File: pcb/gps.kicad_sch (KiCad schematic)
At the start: 16 parts, among them J14 PPS, J15 U.FL, U12 MAX-M10S-00B, U13 TPS22941

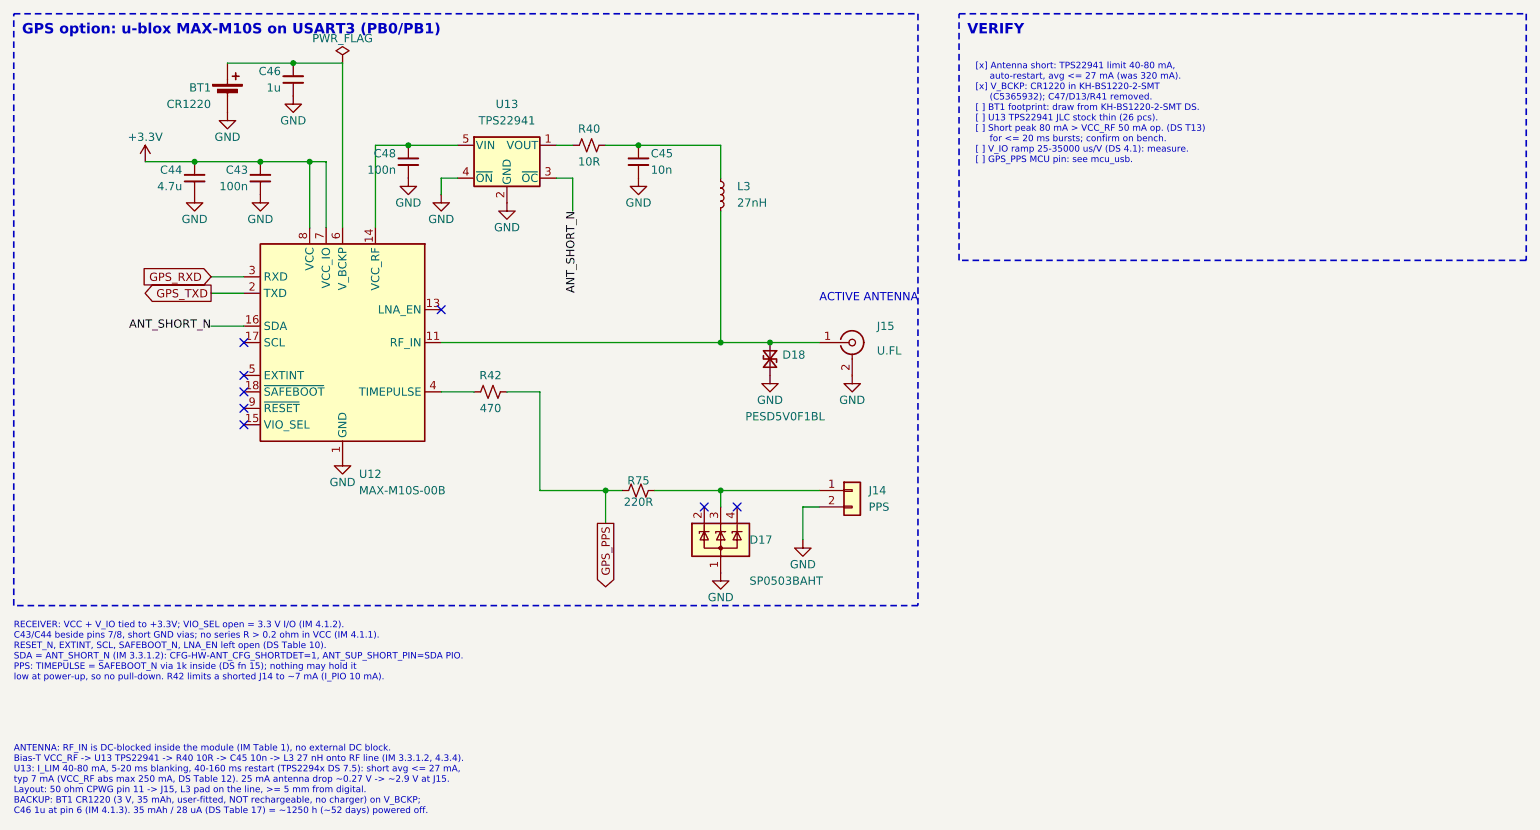
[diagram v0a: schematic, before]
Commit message: Rev C layout: board grown to 130x110 mm, headers J4/J5/J8/J10/J14 removed, power rework layout
- Outline grown 10 mm on top and left edges (130x110 mm); locked edge parts moved with outline
- Removed J4, J5, J8, J10, J14 and support parts (D13-D15, D17, D19, D20, R64-R67, R69-R71, R75-R79); UPDI J13 kept
- Power rework placed and routed (TPS61085 boost, INA193 U14, Q10 soft-start)
- Y1 placed at U9, stray passives moved, silkscreen labels cleaned up
- Routed: DRC 0 errors / 0 unconnected, schematic parity 0, ERC 0; layout gate 11/11
- DRU: ESC_* fine-pitch escape 0.20 mm rule areas, U1 pad-to-pad 0.14 mm
- In2 keep-away waivers (GND-plane shielded): Q2 drain, MCU_TX, MCU_RX near R6, 22.6 mm MCU_RX run near U9
- Libs: 6x6 H13 switch, OLED pin-header module footprint, updated symbols
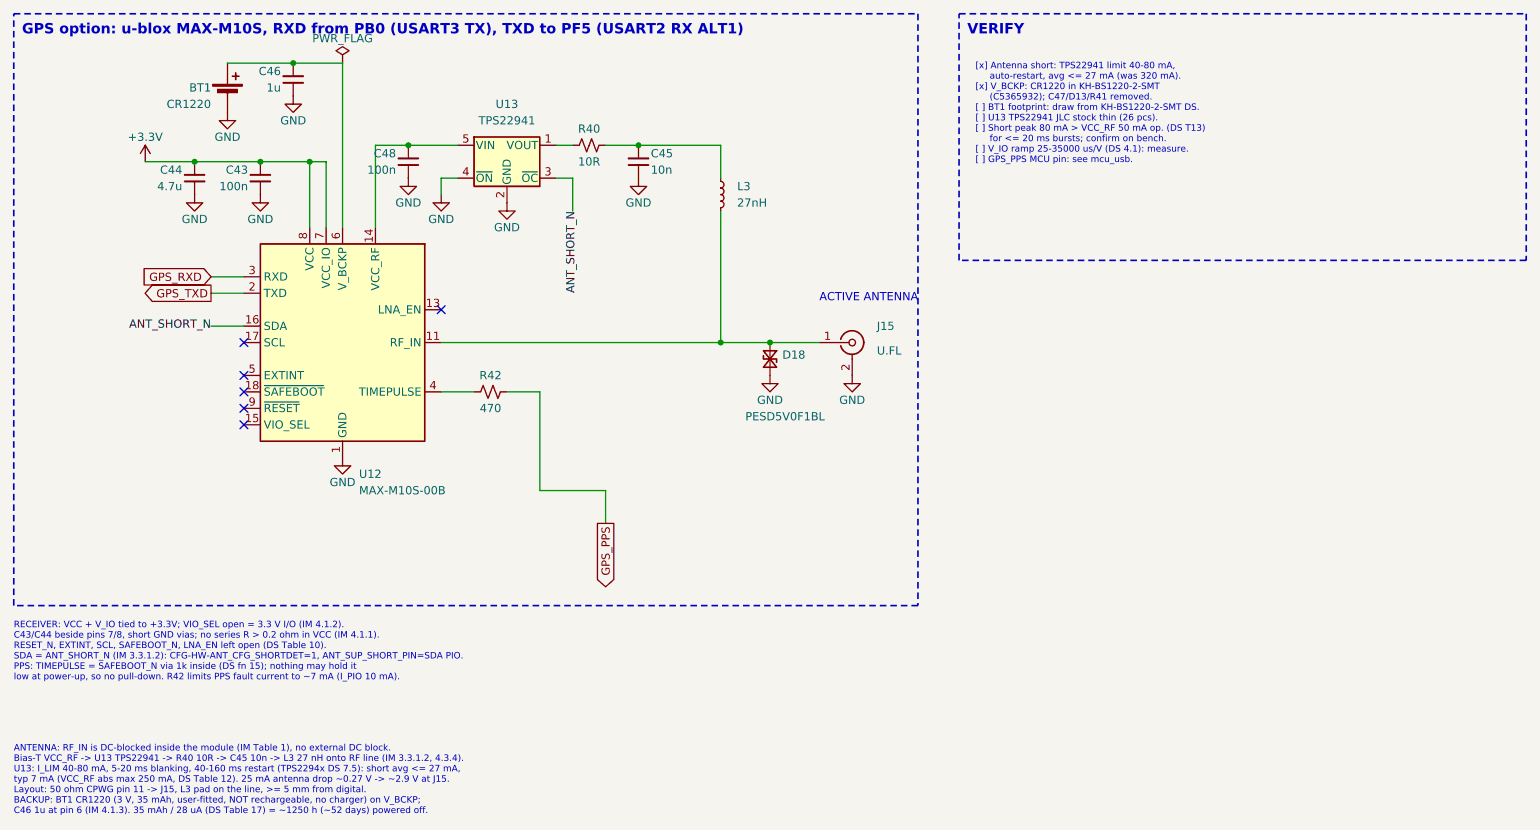
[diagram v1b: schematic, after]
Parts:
- removed D17: SP0503BAHT, Package_TO_SOT_SMD:SOT-143, symbol Power_Protection:SP0503BAHT
- removed J14: PPS, Connector_PinHeader_2.54mm:PinHeader_1x02_P2.54mm_Vertical, symbol Connector_Generic:Conn_01x02
- removed R75: 220R, Resistor_SMD:R_0805_2012Metric, symbol Device:R_Small_US
- C46: footprint Capacitor_SMD:C_0805_2012Metric -> Capacitor_SMD:C_0402_1005Metric; LCSC C28323 -> C52923; MPN CL21B105KBFNNNE -> CL05A105KA5NQNC
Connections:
- no-connect marks 8 -> 6
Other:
- note added: "GPS option: u-blox MAX-M10S, RXD from PB0 (USART3 TX), TXD to PF5 (USART2 RX ALT1)"
- note removed: "GPS option: u-blox MAX-M10S on USART3 (PB0/PB1)"

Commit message: Renumber all references monotonically 1..N per prefix; sync PCB silk labels and auto-named nets; ERC 0, DRC 0/0
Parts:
- renumbered C46 to C103, C48 to C104, C45 to C105, C44 to C106, C43 to C107, D18 to D13, J15 to J8, L3 to L15, R40 to R41, U13 to U10, U12 to U11
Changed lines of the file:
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@@
 		(on_board yes)
 		(dnp no)
-		(property "Reference" "U12"
+		(property "Reference" "U11"
 			(at 104.14 144.78 0)
 			(effects
@@
 			(project "OpenBeacon2"
 				(path "/046319a3-a6ce-4e59-a888-94e340127381/a3f6c2d4-5b7e-4f10-9c8d-2e4b6a8c0d12"
-					(reference "U12")
+					(reference "U11")
 					(unit 1)
 				)
@@
 		(on_board yes)
 		(dnp no)
-		(property "Reference" "C43"
+		(property "Reference" "C107"
 			(at 86.995 97.79 0)
 			(effects
@@
 			(project "OpenBeacon2"
 				(path "/046319a3-a6ce-4e59-a888-94e340127381/a3f6c2d4-5b7e-4f10-9c8d-2e4b6a8c0d12"
-					(reference "C43")
+					(reference "C107")
 					(unit 1)
 				)
@@
 		(on_board yes)
 		(dnp no)
-		(property "Reference" "#PWR1001"
+		(property "Reference" "#PWR116"
 			(at 88.9 101.6 0)
 			(effects
@@
 			(project "OpenBeacon2"
 				(path "/046319a3-a6ce-4e59-a888-94e340127381/a3f6c2d4-5b7e-4f10-9c8d-2e4b6a8c0d12"
-					(reference "#PWR1001")
+					(reference "#PWR116")
 					(unit 1)
 				)
@@
 		(on_board yes)
 		(dnp no)
-		(property "Reference" "C44"
+		(property "Reference" "C106"
 			(at 76.835 97.79 0)
 			(effects
@@
 			(project "OpenBeacon2"
 				(path "/046319a3-a6ce-4e59-a888-94e340127381/a3f6c2d4-5b7e-4f10-9c8d-2e4b6a8c0d12"
-					(reference "C44")
+					(reference "C106")
 					(unit 1)
 				)
@@
 		(on_board yes)
 		(dnp no)
-		(property "Reference" "#PWR1002"
+		(property "Reference" "#PWR115"
 			(at 78.74 101.6 0)
 			(effects
@@
 			(project "OpenBeacon2"
 				(path "/046319a3-a6ce-4e59-a888-94e340127381/a3f6c2d4-5b7e-4f10-9c8d-2e4b6a8c0d12"
-					(reference "#PWR1002")
+					(reference "#PWR115")
 					(unit 1)
 				)
@@
 		(on_board yes)
 		(dnp no)
-		(property "Reference" "#PWR1003"
+		(property "Reference" "#PWR112"
 			(at 71.12 96.52 0)
 			(effects
@@
 			(project "OpenBeacon2"
 				(path "/046319a3-a6ce-4e59-a888-94e340127381/a3f6c2d4-5b7e-4f10-9c8d-2e4b6a8c0d12"
-					(reference "#PWR1003")
+					(reference "#PWR112")
 					(unit 1)
 				)
@@
 		(on_board yes)
 		(dnp no)
-		(property "Reference" "#PWR1004"
+		(property "Reference" "#PWR121"
 			(at 101.6 142.24 0)
 			(effects
@@
 			(project "OpenBeacon2"
 				(path "/046319a3-a6ce-4e59-a888-94e340127381/a3f6c2d4-5b7e-4f10-9c8d-2e4b6a8c0d12"
-					(reference "#PWR1004")
+					(reference "#PWR121")
 					(unit 1)
 				)
@@
 		(on_board yes)
 		(dnp no)
-		(property "Reference" "#FLG905"
+		(property "Reference" "#FLG5"
 			(at 101.6 81.28 0)
 			(effects
@@
 			(project "OpenBeacon2"
 				(path "/046319a3-a6ce-4e59-a888-94e340127381/a3f6c2d4-5b7e-4f10-9c8d-2e4b6a8c0d12"
-					(reference "#FLG905")
+					(reference "#FLG5")
 					(unit 1)
 				)
@@
 		(on_board yes)
 		(dnp no)
-		(property "Reference" "C46"
+		(property "Reference" "C103"
 			(at 92.075 82.55 0)
 			(effects
@@
 			(project "OpenBeacon2"
 				(path "/046319a3-a6ce-4e59-a888-94e340127381/a3f6c2d4-5b7e-4f10-9c8d-2e4b6a8c0d12"
-					(reference "C46")
+					(reference "C103")
 					(unit 1)
 				)
@@
 		(on_board yes)
 		(dnp no)
-		(property "Reference" "#PWR1005"
+		(property "Reference" "#PWR110"
 			(at 93.98 86.36 0)
 			(effects
@@
 			(project "OpenBeacon2"
 				(path "/046319a3-a6ce-4e59-a888-94e340127381/a3f6c2d4-5b7e-4f10-9c8d-2e4b6a8c0d12"
-					(reference "#PWR1005")
+					(reference "#PWR110")
 					(unit 1)
 				)
@@
 		(on_board yes)
 		(dnp no)
-		(property "Reference" "#PWR1006"
+		(property "Reference" "#PWR111"
 			(at 83.82 88.9 0)
 			(effects
@@
 			(project "OpenBeacon2"
 				(path "/046319a3-a6ce-4e59-a888-94e340127381/a3f6c2d4-5b7e-4f10-9c8d-2e4b6a8c0d12"
-					(reference "#PWR1006")
+					(reference "#PWR111")
 					(unit 1)
 				)
@@
 		(on_board yes)
 		(dnp no)
-		(property "Reference" "U13"
+		(property "Reference" "U10"
 			(at 127 87.63 0)
 			(effects
@@
 			(project "OpenBeacon2"
 				(path "/046319a3-a6ce-4e59-a888-94e340127381/a3f6c2d4-5b7e-4f10-9c8d-2e4b6a8c0d12"
-					(reference "U13")
+					(reference "U10")
 					(unit 1)
 				)
@@
 		(on_board yes)
 		(dnp no)
-		(property "Reference" "C48"
+		(property "Reference" "C104"
 			(at 109.855 95.25 0)
 			(effects
@@
 			(project "OpenBeacon2"
 				(path "/046319a3-a6ce-4e59-a888-94e340127381/a3f6c2d4-5b7e-4f10-9c8d-2e4b6a8c0d12"
-					(reference "C48")
+					(reference "C104")
 					(unit 1)
 				)
@@
 		(on_board yes)
 		(dnp no)
-		(property "Reference" "#PWR1007"
+		(property "Reference" "#PWR113"
 			(at 111.76 99.06 0)
 			(effects
@@
 			(project "OpenBeacon2"
 				(path "/046319a3-a6ce-4e59-a888-94e340127381/a3f6c2d4-5b7e-4f10-9c8d-2e4b6a8c0d12"
-					(reference "#PWR1007")
+					(reference "#PWR113")
 					(unit 1)
 				)
@@
 		(on_board yes)
 		(dnp no)
-		(property "Reference" "#PWR1008"
+		(property "Reference" "#PWR117"
 			(at 116.84 101.6 0)
 			(effects
@@
 			(project "OpenBeacon2"
 				(path "/046319a3-a6ce-4e59-a888-94e340127381/a3f6c2d4-5b7e-4f10-9c8d-2e4b6a8c0d12"
-					(reference "#PWR1008")
+					(reference "#PWR117")
 					(unit 1)
 				)
@@
 		(on_board yes)
 		(dnp no)
-		(property "Reference" "#PWR1009"
+		(property "Reference" "#PWR118"
 			(at 127 102.87 0)
 			(effects
@@
 			(project "OpenBeacon2"
 				(path "/046319a3-a6ce-4e59-a888-94e340127381/a3f6c2d4-5b7e-4f10-9c8d-2e4b6a8c0d12"
-					(reference "#PWR1009")
+					(reference "#PWR118")
 					(unit 1)
 				)
@@
 		(on_board yes)
 		(dnp no)
-		(property "Reference" "R40"
+		(property "Reference" "R41"
 			(at 139.7 91.44 90)
 			(effects
@@
 			(project "OpenBeacon2"
 				(path "/046319a3-a6ce-4e59-a888-94e340127381/a3f6c2d4-5b7e-4f10-9c8d-2e4b6a8c0d12"
-					(reference "R40")
+					(reference "R41")
 					(unit 1)
 				)
@@
 		(on_board yes)
 		(dnp no)
-		(property "Reference" "C45"
+		(property "Reference" "C105"
 			(at 149.225 95.25 0)
 			(effects
@@
 			(project "OpenBeacon2"
 				(path "/046319a3-a6ce-4e59-a888-94e340127381/a3f6c2d4-5b7e-4f10-9c8d-2e4b6a8c0d12"
-					(reference "C45")
+					(reference "C105")
 					(unit 1)
 				)
@@
 		(on_board yes)
 		(dnp no)
-		(property "Reference" "#PWR1010"
+		(property "Reference" "#PWR114"
 			(at 147.32 99.06 0)
 			(effects
@@
 			(project "OpenBeacon2"
 				(path "/046319a3-a6ce-4e59-a888-94e340127381/a3f6c2d4-5b7e-4f10-9c8d-2e4b6a8c0d12"
-					(reference "#PWR1010")
+					(reference "#PWR114")
 					(unit 1)
 				)
@@
 		(on_board yes)
 		(dnp no)
-		(property "Reference" "L3"
+		(property "Reference" "L15"
 			(at 162.56 100.33 0)
 			(effects
@@
 			(project "OpenBeacon2"
 				(path "/046319a3-a6ce-4e59-a888-94e340127381/a3f6c2d4-5b7e-4f10-9c8d-2e4b6a8c0d12"
-					(reference "L3")
+					(reference "L15")
 					(unit 1)
 				)
@@
 		(on_board yes)
 		(dnp no)
-		(property "Reference" "J15"
+		(property "Reference" "J8"
 			(at 184.15 121.92 0)
 			(effects
@@
 			(project "OpenBeacon2"
 				(path "/046319a3-a6ce-4e59-a888-94e340127381/a3f6c2d4-5b7e-4f10-9c8d-2e4b6a8c0d12"
-					(reference "J15")
+					(reference "J8")
 					(unit 1)
 				)
@@
 		(on_board yes)
 		(dnp no)
-		(property "Reference" "#PWR1011"
+		(property "Reference" "#PWR120"
 			(at 180.34 129.54 0)
 			(effects
@@
 			(project "OpenBeacon2"
 				(path "/046319a3-a6ce-4e59-a888-94e340127381/a3f6c2d4-5b7e-4f10-9c8d-2e4b6a8c0d12"
-					(reference "#PWR1011")
+					(reference "#PWR120")
 					(unit 1)
 				)
@@
 		(on_board yes)
 		(dnp no)
-		(property "Reference" "D18"
+		(property "Reference" "D13"
 			(at 169.545 126.365 90)
 			(effects
@@
 			(project "OpenBeacon2"
 				(path "/046319a3-a6ce-4e59-a888-94e340127381/a3f6c2d4-5b7e-4f10-9c8d-2e4b6a8c0d12"
-					(reference "D18")
+					(reference "D13")
 					(unit 1)
 				)
@@
 		(on_board yes)
 		(dnp no)
-		(property "Reference" "#PWR943"
+		(property "Reference" "#PWR119"
 			(at 167.64 129.54 0)
 			(effects
@@
 			(project "OpenBeacon2"
 				(path "/046319a3-a6ce-4e59-a888-94e340127381/a3f6c2d4-5b7e-4f10-9c8d-2e4b6a8c0d12"
-					(reference "#PWR943")
-					(unit 1)
-				)
+					(reference "#PWR119")
+					(unit 1)
+				)
